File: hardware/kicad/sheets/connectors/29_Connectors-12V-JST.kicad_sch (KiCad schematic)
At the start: 35 parts, among them U32 VH3_96-2P_WZ, U70 VH3_96-2P_WZ, U71 VH3_96-2P_WZ

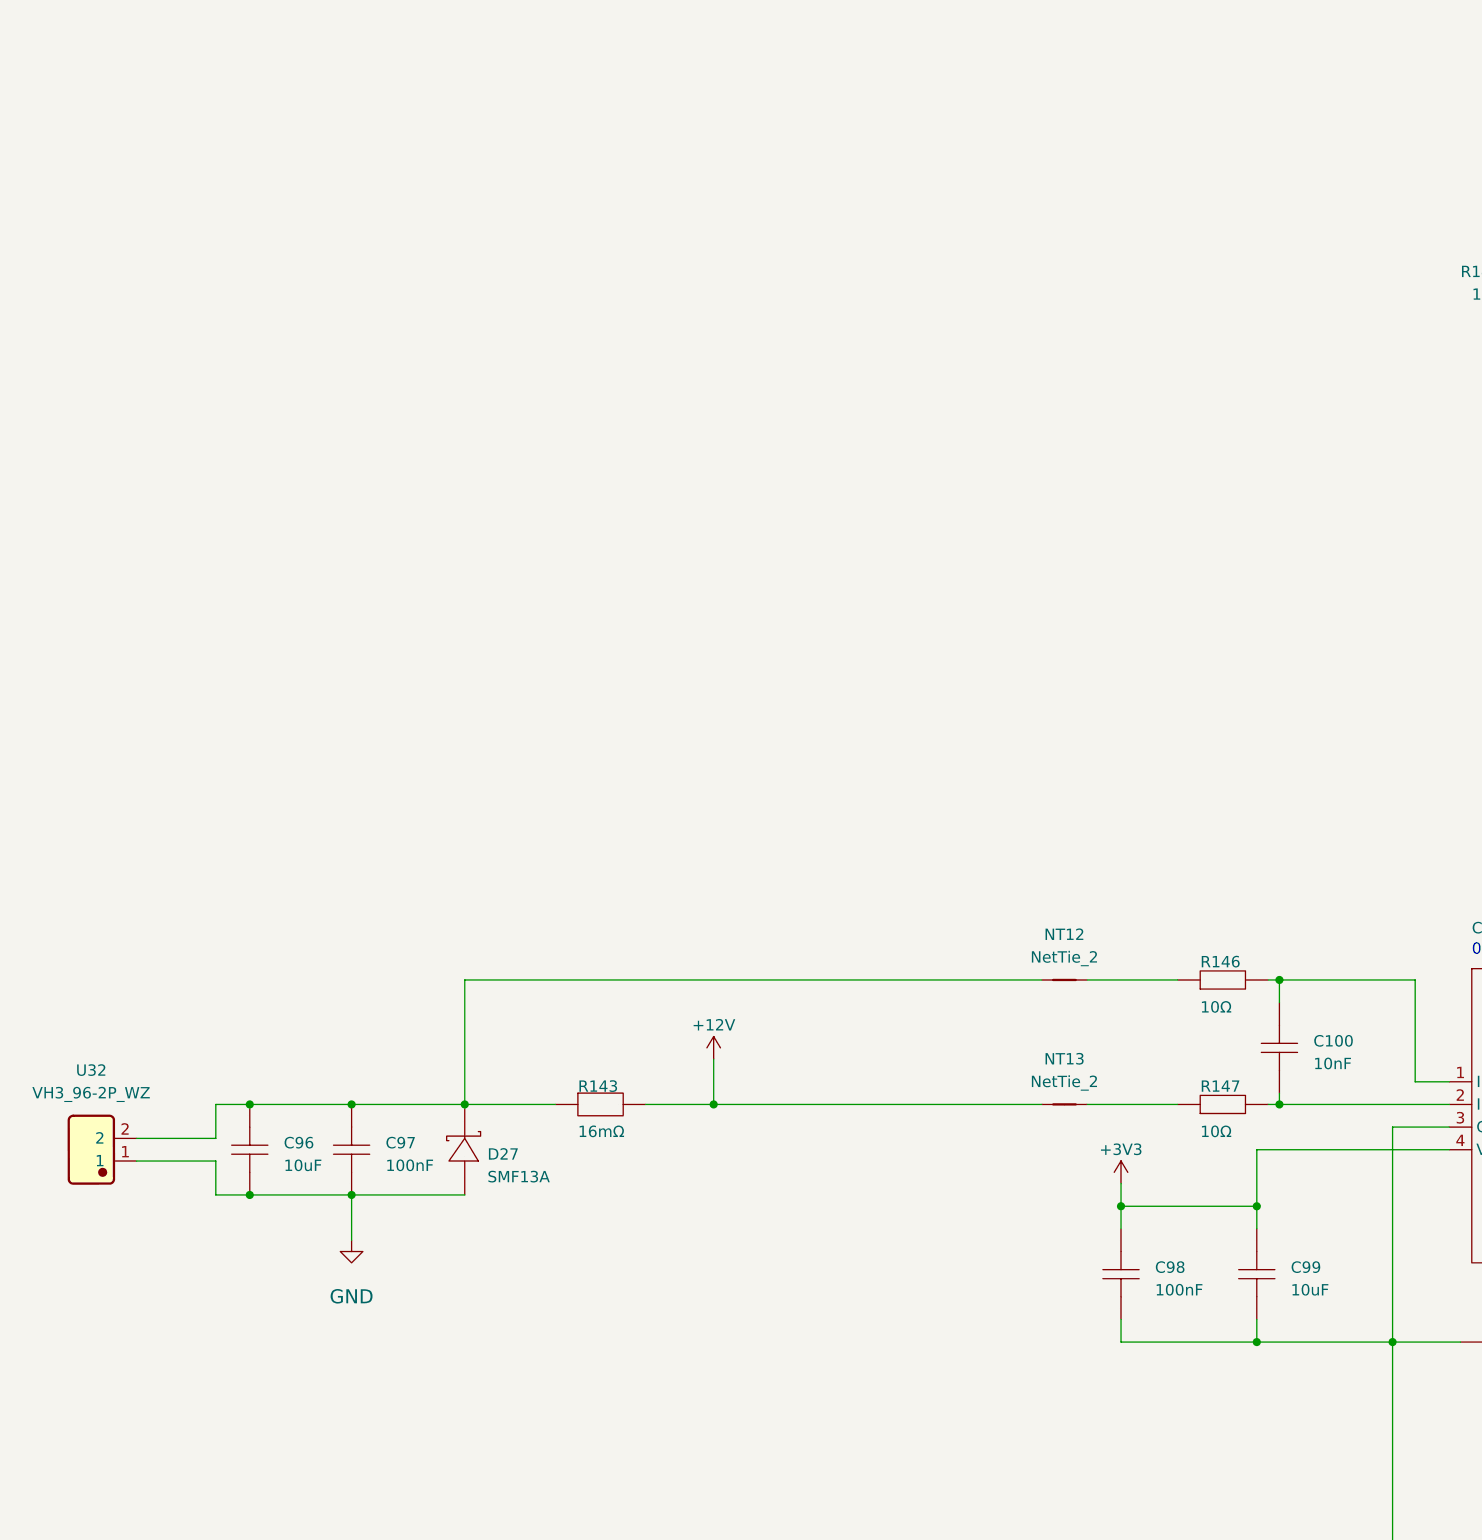
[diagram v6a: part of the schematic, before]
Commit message: sheet optimized ports and current sensor
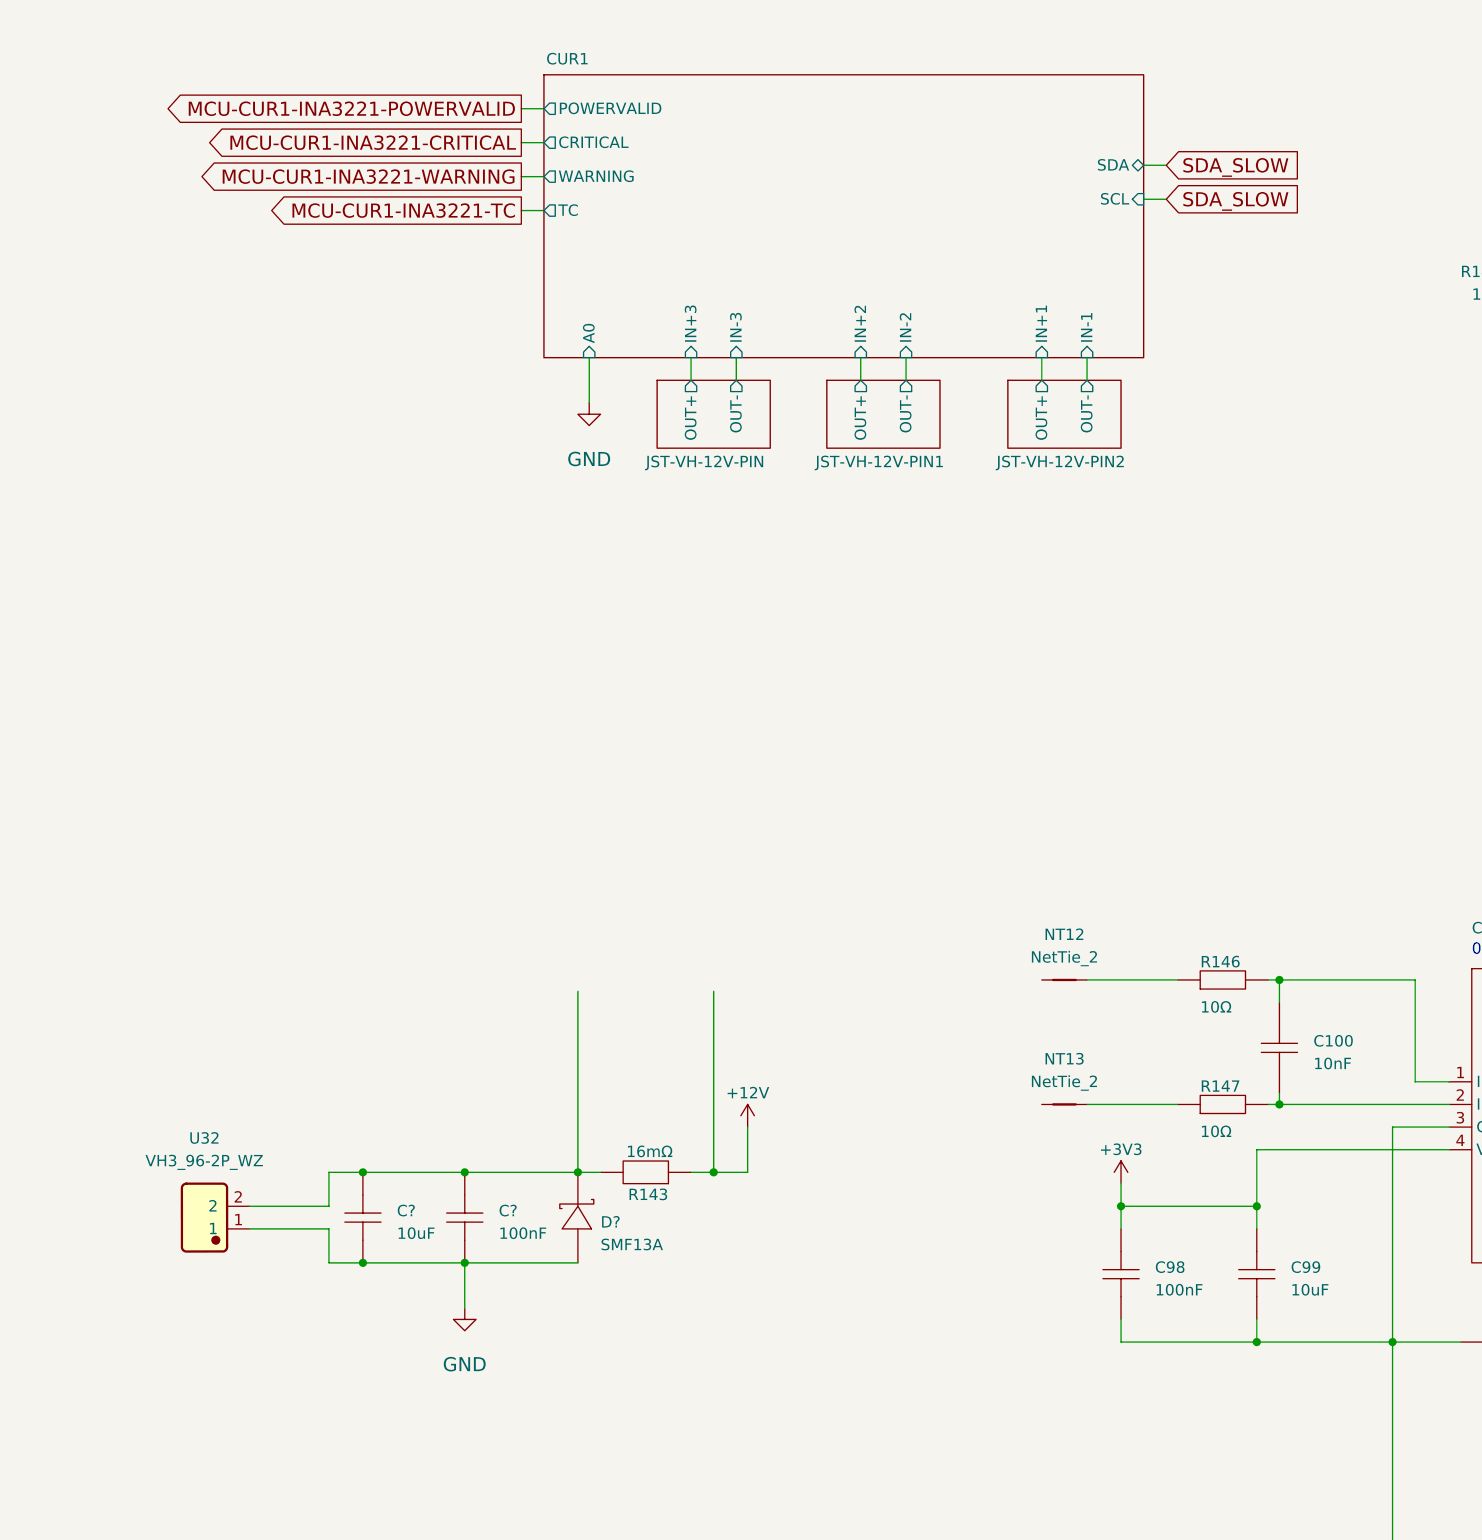
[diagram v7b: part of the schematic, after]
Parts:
- renumbered C97 to C?, C96 to C?, D27 to D?
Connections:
- net +12V: now also R143.1; no longer NT13.1, R143.2
- net at C?.2, C?.2, D?.1 (K)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: now also R143.2; no longer NT12.1, R143.1
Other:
- added sheet CUR1 (MISC_IO_CURR_SENSING_1.kicad_sch)
- added sheet JST-VH-12V-PIN (JST-VH-12V-PIN.kicad_sch)
- added sheet JST-VH-12V-PIN1 (JST-VH-12V-PIN.kicad_sch)
- added sheet JST-VH-12V-PIN2 (JST-VH-12V-PIN.kicad_sch)
- moved on the sheet: C?, D?, U32

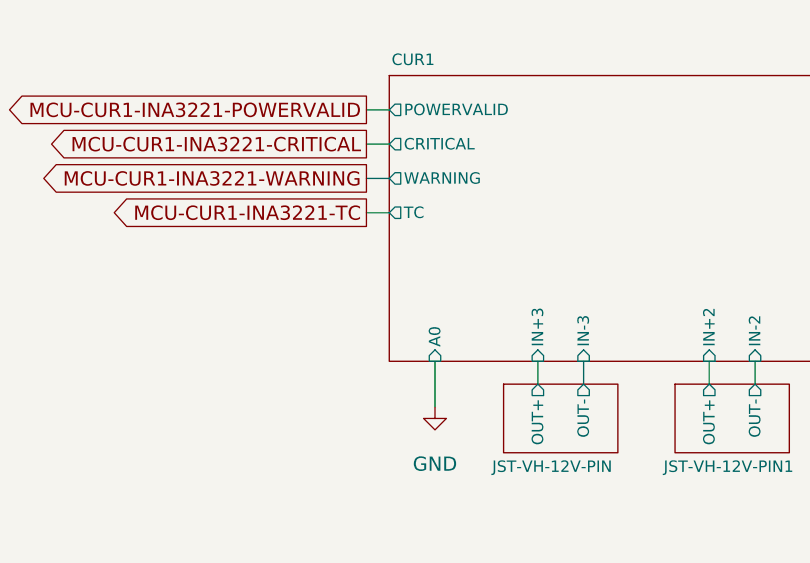
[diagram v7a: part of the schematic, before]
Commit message: more sheet simplfiication and pre simpler 12v sym
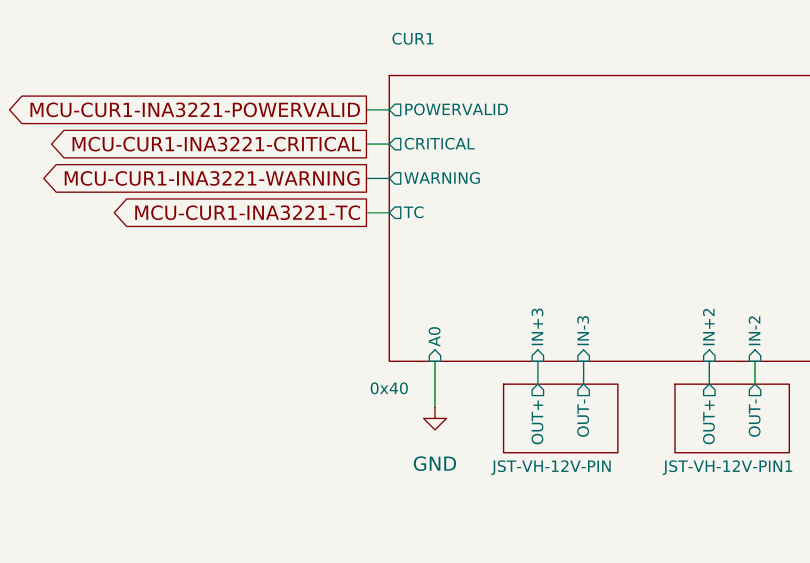
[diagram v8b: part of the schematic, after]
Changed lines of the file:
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@@
 		)
 		(property "Sheetname" "CUR1"
-			(at 73.914 24.384 0)
+			(at 73.914 22.098 0)
 			(effects
 				(font
@@
 			)
 		)
+		(property "i2c Address" "0x40"
+			(at 73.66 60.198 0)
+			(effects
+				(font
+					(size 1.27 1.27)
+				)
+			)
+		)
